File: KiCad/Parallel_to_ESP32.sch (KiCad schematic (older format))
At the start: 10 parts, among them J1 DB25_Male, J2 Micro_SD_Card_Socket, U1 ESP32-DEVKIT-V1, U2 SN74CB3T16210

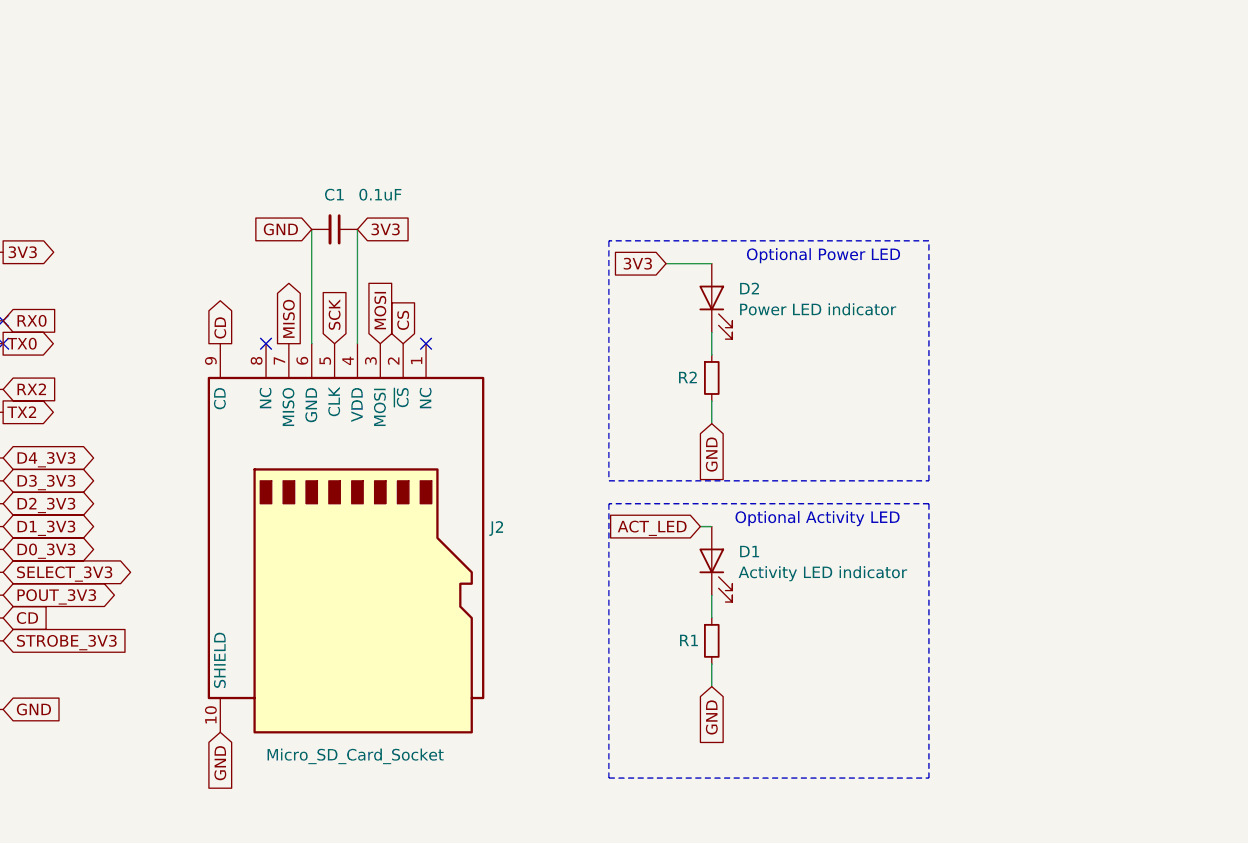
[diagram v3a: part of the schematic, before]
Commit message: Added pinheader for UART1
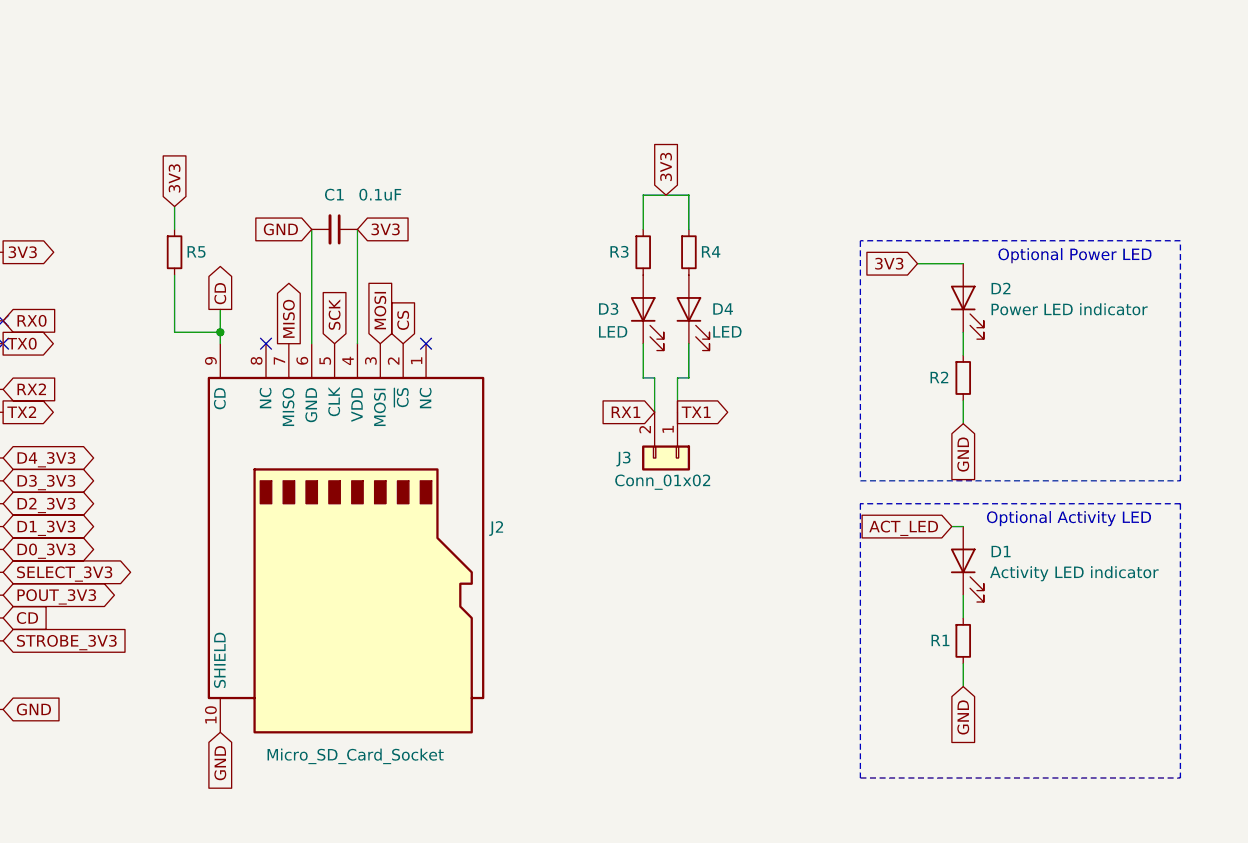
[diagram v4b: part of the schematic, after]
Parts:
- added D3, D4: LED, Diode_SMD:D_0603_1608Metric_Pad1.05x0.95mm_HandSolder, symbol Device:LED
- added J3: Conn_01x02, Connector_PinHeader_2.54mm:PinHeader_1x02_P2.54mm_Vertical, symbol Connector_Generic:Conn_01x02
- added R3, R4, R5: 1k, Resistor_SMD:R_0603_1608Metric_Pad1.05x0.95mm_HandSolder, symbol Device:R_Small
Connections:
- net +3V3: now also R3.1, R4.1, R5.1
- net CD: now also R5.2
- net RX1: now also D3.1 (K), J3.2 (Pin_2)
- net TX1: now also D4.1 (K), J3.1 (Pin_1)
- new net: D3.2 (A), R3.2
- new net: D4.2 (A), R4.2
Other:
- moved on the sheet: D1, D2, R1, R2
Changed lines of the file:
@@
 L Device:LED D2
 U 1 1 5EBAFFCE
-P 9000 3400
-F 0 "D2" V 9039 3283 50  0000 R CNN
-F 1 "Power LED indicator" V 8948 3283 50  0000 R CNN
-F 2 "LED_THT:LED_D3.0mm" H 9000 3400 50  0001 C CNN
-F 3 "~" H 9000 3400 50  0001 C CNN
-	1    9000 3400
+P 10100 3400
+F 0 "D2" V 10139 3283 50  0000 R CNN
+F 1 "Power LED indicator" V 10048 3283 50  0000 R CNN
+F 2 "LED_THT:LED_D3.0mm" H 10100 3400 50  0001 C CNN
+F 3 "~" H 10100 3400 50  0001 C CNN
+	1    10100 3400
 	0    -1   -1   0
 $EndComp
-Text GLabel 9000 3950 3    50   Input ~ 0
-GND
-Wire Wire Line
-	8800 3250 9000 3250
-Wire Wire Line
-	9000 3850 9000 3950
+Text GLabel 10100 3950 3    50   Input ~ 0
+GND
+Wire Wire Line
+	9900 3250 10100 3250
+Wire Wire Line
+	10100 3850 10100 3950
 Text GLabel 1550 3600 0    50   Input ~ 0
 ACK
@@
 L Device:R_Small R2
 U 1 1 5EB9BBF1
-P 9000 3750
-F 0 "R2" H 8850 3750 50  0000 L CNN
-F 1 "150" H 9050 3750 50  0001 L CNN
-F 2 "Resistor_SMD:R_1206_3216Metric_Pad1.42x1.75mm_HandSolder" H 9000 3750 50  0001 C CNN
-F 3 "~" H 9000 3750 50  0001 C CNN
-	1    9000 3750
+P 10100 3750
+F 0 "R2" H 9950 3750 50  0000 L CNN
+F 1 "150" H 10150 3750 50  0001 L CNN
+F 2 "Resistor_SMD:R_1206_3216Metric_Pad1.42x1.75mm_HandSolder" H 10100 3750 50  0001 C CNN
+F 3 "~" H 10100 3750 50  0001 C CNN
+	1    10100 3750
 	1    0    0    -1
 $EndComp
@@
 L Device:R_Small R1
 U 1 1 5EB9CA00
-P 9000 4900
-F 0 "R1" H 8900 4900 50  0000 C CNN
-F 1 "150" H 9150 4900 50  0001 C CNN
-F 2 "Resistor_SMD:R_1206_3216Metric_Pad1.42x1.75mm_HandSolder" H 9000 4900 50  0001 C CNN
-F 3 "~" H 9000 4900 50  0001 C CNN
-	1    9000 4900
+P 10100 4900
+F 0 "R1" H 10000 4900 50  0000 C CNN
+F 1 "150" H 10250 4900 50  0001 C CNN
+F 2 "Resistor_SMD:R_1206_3216Metric_Pad1.42x1.75mm_HandSolder" H 10100 4900 50  0001 C CNN
+F 3 "~" H 10100 4900 50  0001 C CNN
+	1    10100 4900
 	1    0    0    -1
 $EndComp
@@
 L Device:LED D1
 U 1 1 5EBA7223
-P 9000 4550
-F 0 "D1" V 9039 4433 50  0000 R CNN
-F 1 "Activity LED indicator" V 8948 4433 50  0000 R CNN
-F 2 "LED_THT:LED_D3.0mm" H 9000 4550 50  0001 C CNN
-F 3 "~" H 9000 4550 50  0001 C CNN
-	1    9000 4550
+P 10100 4550
+F 0 "D1" V 10139 4433 50  0000 R CNN
+F 1 "Activity LED indicator" V 10048 4433 50  0000 R CNN
+F 2 "LED_THT:LED_D3.0mm" H 10100 4550 50  0001 C CNN
+F 3 "~" H 10100 4550 50  0001 C CNN
+	1    10100 4550
 	0    -1   -1   0
 $EndComp
-Text Notes 9100 4400 0    50   ~ 0
+Text Notes 10200 4400 0    50   ~ 0
 Optional Activity LED
 Wire Notes Line
-	8550 3150 8550 4200
-Wire Notes Line
-	8550 4200 9950 4200
-Wire Notes Line
-	9950 4200 9950 3150
-Wire Notes Line
-	9950 3150 8550 3150
-Text Notes 9150 3250 0    50   ~ 0
+	9650 3150 9650 4200
+Wire Notes Line
+	9650 4200 11050 4200
+Wire Notes Line
+	11050 4200 11050 3150
+Wire Notes Line
+	11050 3150 9650 3150
+Text Notes 10250 3250 0    50   ~ 0
 Optional Power LED
 Wire Wire Line
@@
 Text GLabel 7650 3600 1    50   Input ~ 0
 CS
-Text GLabel 6850 3600 1    50   Output ~ 0
+Text GLabel 6850 3450 1    50   Output ~ 0
 CD
 Wire Wire Line
-	9000 4700 9000 4800
-Wire Wire Line
-	9000 5000 9000 5100
-Wire Notes Line
-	8550 5500 9950 5500
-Wire Notes Line
-	9950 4300 8550 4300
+	10100 4700 10100 4800
+Wire Wire Line
+	10100 5000 10100 5100
+Wire Notes Line
+	9650 5500 11050 5500
+Wire Notes Line
+	11050 4300 9650 4300
 Text GLabel 5900 4800 2    50   Input ~ 0
 CD
 Text GLabel 4700 4100 0    50   Output ~ 0
 CS
-Text GLabel 8950 4400 0    50   Input ~ 0
+Text GLabel 10050 4400 0    50   Input ~ 0
 ACT_LED
 Wire Notes Line
-	9950 4300 9950 5500
-Wire Notes Line
-	8550 4300 8550 5500
+	11050 4300 11050 5500
+Wire Notes Line
+	9650 4300 9650 5500
 $Comp
 L Device:C_Small C1
@@
 	1    0    0    -1
 $EndComp
-Text GLabel 8800 3250 0    50   Input ~ 0
+Text GLabel 9900 3250 0    50   Input ~ 0
 3V3
 Text GLabel 2750 3750 0    50   Input ~ 0
@@
 NoConn ~ 5900 3600
 Wire Wire Line
-	9000 3650 9000 3550
-Wire Wire Line
-	8950 4400 9000 4400
-Text GLabel 9000 5100 3    50   Input ~ 0
+	10100 3650 10100 3550
+Wire Wire Line
+	10050 4400 10100 4400
+Text GLabel 10100 5100 3    50   Input ~ 0
 GND
 Text GLabel 4700 3500 0    50   Input ~ 0
@@
 Text GLabel 3750 3050 2    50   Input ~ 0
 GND
+$Comp
+L Connector_Generic:Conn_01x02 J3
+U 1 1 645092AA
+P 8850 4100
+F 0 "J3" V 8850 3900 50  0000 R CNN
+F 1 "Conn_01x02" V 8950 4250 50  0000 R CNN
+F 2 "Connector_PinHeader_2.54mm:PinHeader_1x02_P2.54mm_Vertical" H 8850 4100 50  0001 C CNN
+F 3 "~" H 8850 4100 50  0001 C CNN
+	1    8850 4100
+	0    1    1    0
+$EndComp
+Text GLabel 8850 3900 2    50   Output ~ 0
+TX1
+Text GLabel 8750 3900 0    50   Input ~ 0
+RX1
+$Comp
+L Device:LED D3
+U 1 1 64514543
+P 8700 3450
+F 0 "D3" V 8700 3650 50  0000 R CNN
+F 1 "LED" V 8600 3650 50  0000 R CNN
+F 2 "Diode_SMD:D_0603_1608Metric_Pad1.05x0.95mm_HandSolder" H 8700 3450 50  0001 C CNN
+F 3 "~" H 8700 3450 50  0001 C CNN
+	1    8700 3450
+	0    -1   -1   0
+$EndComp
+$Comp
+L Device:R_Small R3
+U 1 1 645152F1
+P 8700 3200
+F 0 "R3" H 8550 3200 50  0000 L CNN
+F 1 "1k" H 8750 3200 50  0001 L CNN
+F 2 "Resistor_SMD:R_0603_1608Metric_Pad1.05x0.95mm_HandSolder" H 8700 3200 50  0001 C CNN
+F 3 "~" H 8700 3200 50  0001 C CNN
+	1    8700 3200
+	1    0    0    -1
+$EndComp
+Text GLabel 8800 2950 1    50   Input ~ 0
+3V3
+$Comp
+L Device:LED D4
+U 1 1 6452D76C
+P 8900 3450
+F 0 "D4" V 8900 3350 50  0000 R CNN
+F 1 "LED" V 8800 3350 50  0000 R CNN
+F 2 "Diode_SMD:D_0603_1608Metric_Pad1.05x0.95mm_HandSolder" H 8900 3450 50  0001 C CNN
+F 3 "~" H 8900 3450 50  0001 C CNN
+	1    8900 3450
+	0    -1   -1   0
+$EndComp
+$Comp
+L Device:R_Small R4
+U 1 1 6452D776
+P 8900 3200
+F 0 "R4" H 8950 3200 50  0000 L CNN
+F 1 "1k" H 8950 3200 50  0001 L CNN
+F 2 "Resistor_SMD:R_0603_1608Metric_Pad1.05x0.95mm_HandSolder" H 8900 3200 50  0001 C CNN
+F 3 "~" H 8900 3200 50  0001 C CNN
+	1    8900 3200
+	1    0    0    -1
+$EndComp
+Wire Wire Line
+	8700 3100 8700 2950
+Wire Wire Line
+	8900 3100 8900 2950
+Wire Wire Line
+	8700 2950 8900 2950
+Wire Wire Line
+	8700 3600 8700 3750
+Wire Wire Line
+	8700 3750 8750 3750
+Wire Wire Line
+	8750 3750 8750 3900
+Wire Wire Line
+	8850 3900 8850 3750
+Wire Wire Line
+	8850 3750 8900 3750
+Wire Wire Line
+	8900 3600 8900 3750
+$Comp
+L Device:R_Small R5
+U 1 1 64555336
+P 6650 3200
+F 0 "R5" H 6700 3200 50  0000 L CNN
+F 1 "1k" H 6700 3200 50  0001 L CNN
+F 2 "Resistor_SMD:R_0603_1608Metric_Pad1.05x0.95mm_HandSolder" H 6650 3200 50  0001 C CNN
+F 3 "~" H 6650 3200 50  0001 C CNN
+	1    6650 3200
+	1    0    0    -1
+$EndComp
+Text GLabel 6650 3000 1    50   Input ~ 0
+3V3
+Wire Wire Line
+	6850 3600 6850 3550
+Wire Wire Line
+	6650 3300 6650 3550
+Wire Wire Line
+	6650 3550 6850 3550
+Connection ~ 6850 3550
+Wire Wire Line
+	6850 3550 6850 3450
+Wire Wire Line
+	6650 3100 6650 3000
 $EndSCHEMATC

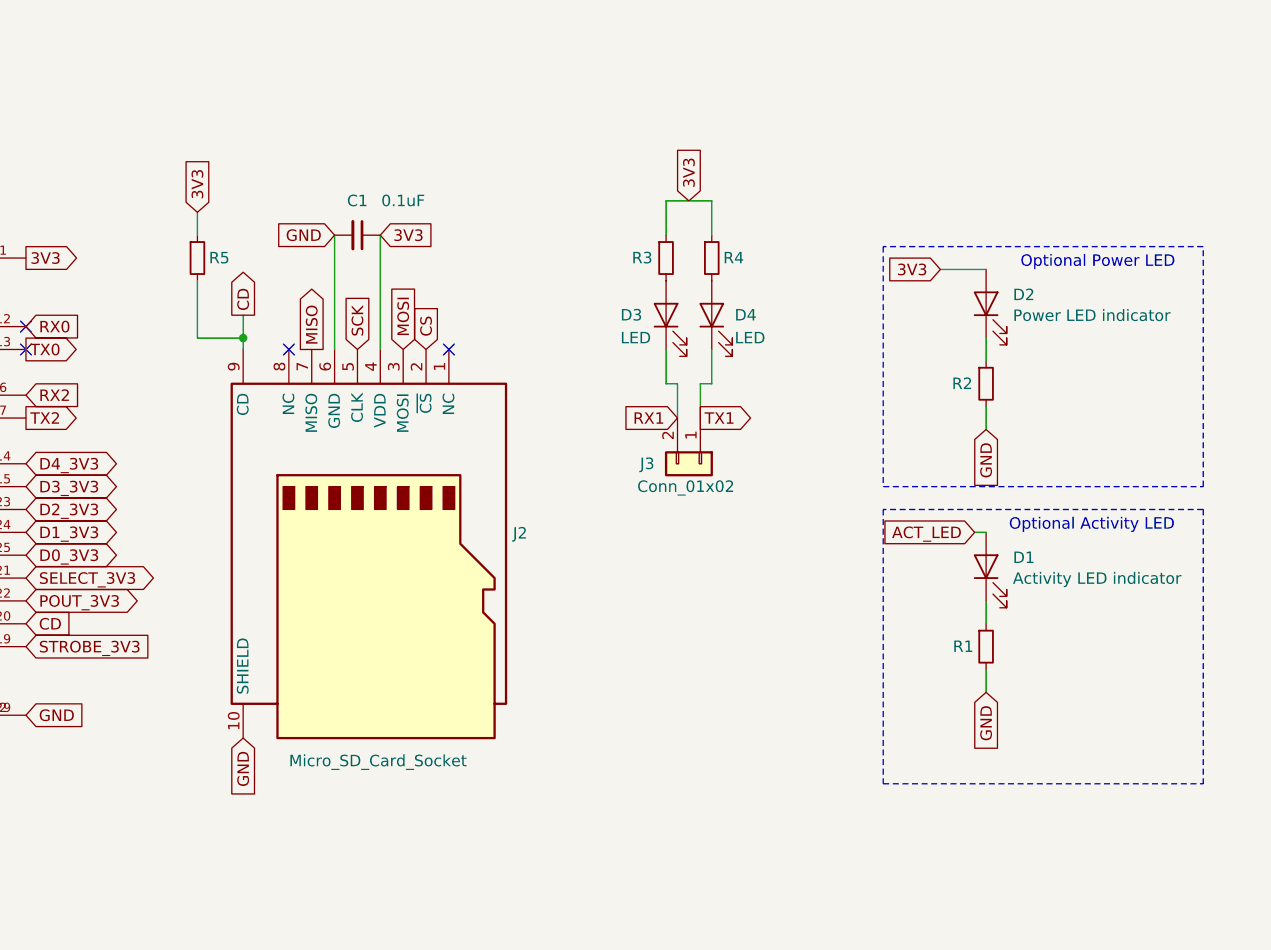
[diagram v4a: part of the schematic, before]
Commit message: Added pinheader for UART2
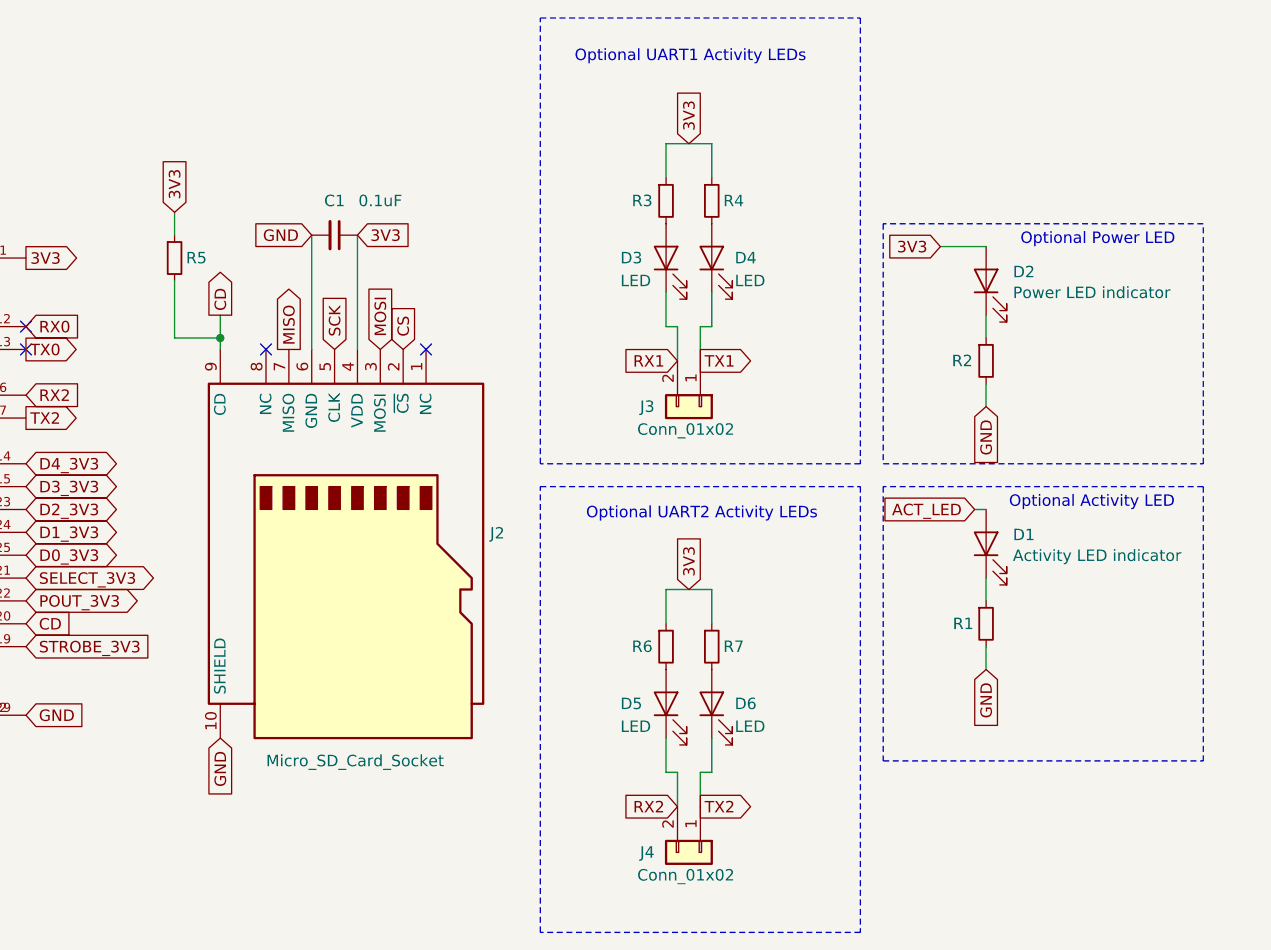
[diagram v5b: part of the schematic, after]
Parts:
- added D5, D6: LED, Diode_SMD:D_0603_1608Metric_Pad1.05x0.95mm_HandSolder, symbol Device:LED
- added J4: Conn_01x02, Connector_PinHeader_2.54mm:PinHeader_1x02_P2.54mm_Vertical, symbol Connector_Generic:Conn_01x02
- added R6, R7: 1k, Resistor_SMD:R_0603_1608Metric_Pad1.05x0.95mm_HandSolder, symbol Device:R_Small
- R5: value 1k -> 10k
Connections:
- net +3V3: now also R6.1, R7.1
- net RX2: now also D5.1 (K), J4.2 (Pin_2)
- net TX2: now also D6.1 (K), J4.1 (Pin_1)
- new net: D5.2 (A), R6.2
- new net: D6.2 (A), R7.2
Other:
- note added: "Optional UART1 Activity LEDs"
- note added: "Optional UART2 Activity LEDs"
- moved on the sheet: C1, D1, D2, D3, D4, J2, J3, R1, R2, R3, R4, R5

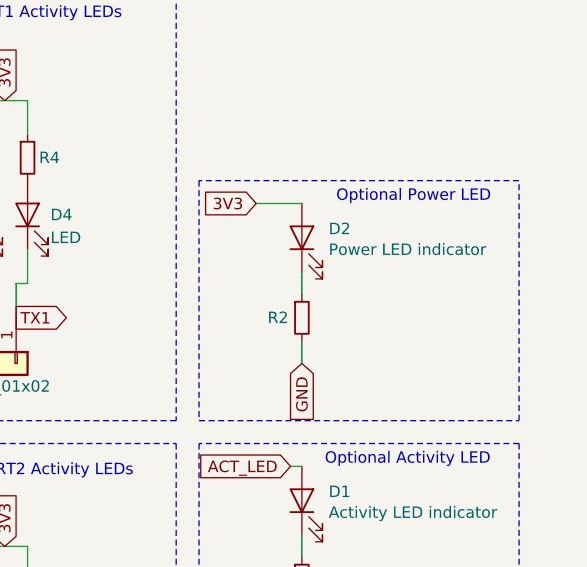
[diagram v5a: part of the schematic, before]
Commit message: Changed R2 resistor to 0805-footprint and did some routing fixes
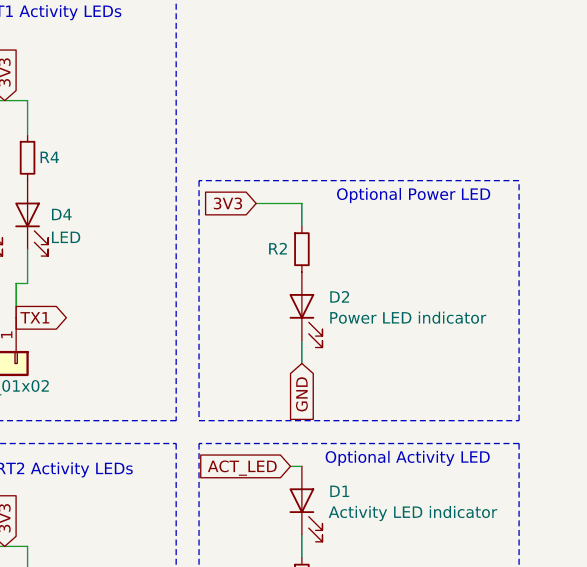
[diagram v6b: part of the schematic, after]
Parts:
- R2: footprint Resistor_SMD:R_1206_3216Metric_Pad1.42x1.75mm_HandSolder -> Resistor_SMD:R_0805_2012Metric_Pad1.15x1.40mm_HandSolder
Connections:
- net +3V3: now also R2.1; no longer D2.2 (A)
- net GND: now also D2.1 (K); no longer R2.2
- new net: D2.2 (A), R2.2
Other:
- moved on the sheet: D2, R2
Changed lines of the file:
@@
 L Device:LED D2
 U 1 1 5EBAFFCE
-P 10100 3300
-F 0 "D2" V 10139 3183 50  0000 R CNN
-F 1 "Power LED indicator" V 10048 3183 50  0000 R CNN
-F 2 "LED_THT:LED_D3.0mm" H 10100 3300 50  0001 C CNN
-F 3 "~" H 10100 3300 50  0001 C CNN
-	1    10100 3300
+P 10100 3600
+F 0 "D2" V 10139 3483 50  0000 R CNN
+F 1 "Power LED indicator" V 10048 3483 50  0000 R CNN
+F 2 "LED_THT:LED_D3.0mm" H 10100 3600 50  0001 C CNN
+F 3 "~" H 10100 3600 50  0001 C CNN
+	1    10100 3600
 	0    -1   -1   0
 $EndComp
@@
 Wire Wire Line
 	9900 3150 10100 3150
-Wire Wire Line
-	10100 3750 10100 3850
 Text GLabel 1550 3600 0    50   Input ~ 0
 ACK
@@
 L Device:R_Small R2
 U 1 1 5EB9BBF1
-P 10100 3650
-F 0 "R2" H 9950 3650 50  0000 L CNN
-F 1 "150" H 10150 3650 50  0001 L CNN
-F 2 "Resistor_SMD:R_1206_3216Metric_Pad1.42x1.75mm_HandSolder" H 10100 3650 50  0001 C CNN
-F 3 "~" H 10100 3650 50  0001 C CNN
-	1    10100 3650
-	1    0    0    -1
-$EndComp
-$Comp
-L Device:R_Small R1
-U 1 1 5EB9CA00
-P 10100 4800
-F 0 "R1" H 10000 4800 50  0000 C CNN
-F 1 "150" H 10250 4800 50  0001 C CNN
-F 2 "Resistor_SMD:R_1206_3216Metric_Pad1.42x1.75mm_HandSolder" H 10100 4800 50  0001 C CNN
-F 3 "~" H 10100 4800 50  0001 C CNN
-	1    10100 4800
-	1    0    0    -1
-$EndComp
-$Comp
-L Device:LED D1
-U 1 1 5EBA7223
-P 10100 4450
-F 0 "D1" V 10139 4333 50  0000 R CNN
-F 1 "Activity LED indicator" V 10048 4333 50  0000 R CNN
-F 2 "LED_THT:LED_D3.0mm" H 10100 4450 50  0001 C CNN
-F 3 "~" H 10100 4450 50  0001 C CNN
-	1    10100 4450
-	0    -1   -1   0
+P 10100 3350
+F 0 "R2" H 9950 3350 50  0000 L CNN
+F 1 "150" H 10150 3350 50  0001 L CNN
+F 2 "Resistor_SMD:R_0805_2012Metric_Pad1.15x1.40mm_HandSolder" H 10100 3350 50  0001 C CNN
+F 3 "~" H 10100 3350 50  0001 C CNN
+	1    10100 3350
+	1    0    0    -1
 $EndComp
 Text Notes 10200 4300 0    50   ~ 0
@@
 Text GLabel 6750 3450 1    50   Output ~ 0
 CD
-Wire Wire Line
-	10100 4600 10100 4700
-Wire Wire Line
-	10100 4900 10100 5000
 Wire Notes Line
 	9650 5400 11050 5400
@@
 NoConn ~ 5900 3600
 Wire Wire Line
-	10100 3550 10100 3450
-Wire Wire Line
 	10050 4300 10100 4300
-Text GLabel 10100 5000 3    50   Input ~ 0
-GND
 Text GLabel 4700 3500 0    50   Input ~ 0
 RX1
@@
 Text Notes 8350 4350 0    50   ~ 0
 Optional UART2 Activity LEDs
+Wire Wire Line
+	10100 3150 10100 3250
+Wire Wire Line
+	10100 3850 10100 3750
+Text GLabel 10100 5000 3    50   Input ~ 0
+GND
+Wire Wire Line
+	10100 4900 10100 5000
+Wire Wire Line
+	10100 4600 10100 4700
+$Comp
+L Device:LED D1
+U 1 1 5EBA7223
+P 10100 4450
+F 0 "D1" V 10139 4333 50  0000 R CNN
+F 1 "Activity LED indicator" V 10048 4333 50  0000 R CNN
+F 2 "LED_THT:LED_D3.0mm" H 10100 4450 50  0001 C CNN
+F 3 "~" H 10100 4450 50  0001 C CNN
+	1    10100 4450
+	0    -1   -1   0
+$EndComp
+$Comp
+L Device:R_Small R1
+U 1 1 5EB9CA00
+P 10100 4800
+F 0 "R1" H 10000 4800 50  0000 C CNN
+F 1 "150" H 10250 4800 50  0001 C CNN
+F 2 "Resistor_SMD:R_1206_3216Metric_Pad1.42x1.75mm_HandSolder" H 10100 4800 50  0001 C CNN
+F 3 "~" H 10100 4800 50  0001 C CNN
+	1    10100 4800
+	1    0    0    -1
+$EndComp
 $EndSCHEMATC
